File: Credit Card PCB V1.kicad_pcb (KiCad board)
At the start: 2 copper layers, 85.5 x 54 mm, 53 parts, among them J1 USB_C_Receptacle_USB2.0, SW0 SW_Push, SW1 RotaryEncoder, U1 USBLC6-2SC6, U2 ATmega32U2-A, Y1 16MHz

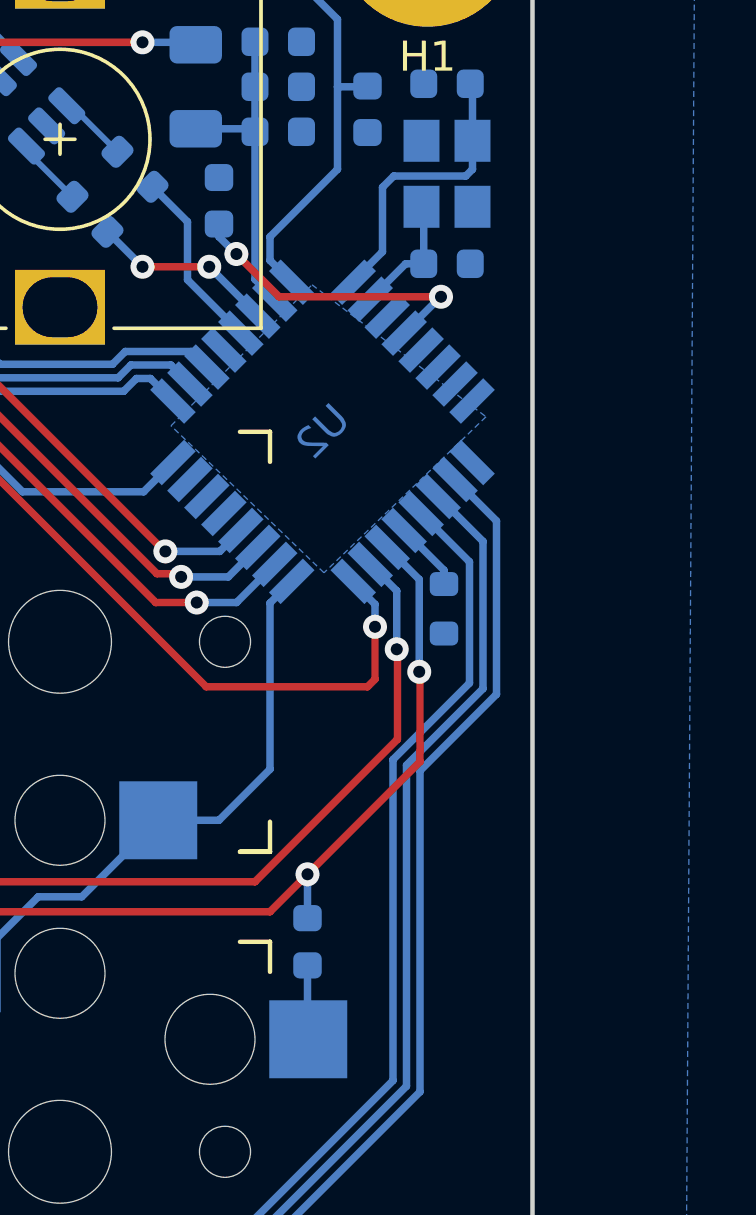
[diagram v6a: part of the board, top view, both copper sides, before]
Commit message: Adding slikscreen logo
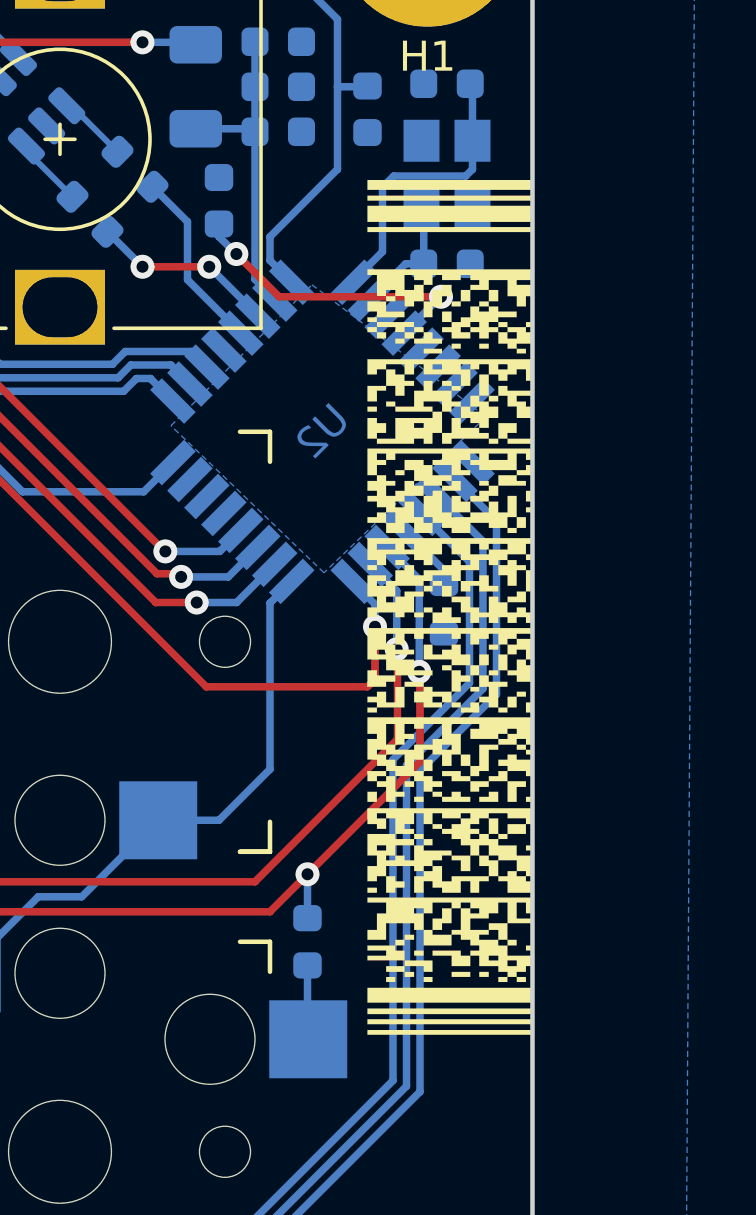
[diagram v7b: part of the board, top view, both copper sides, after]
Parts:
- added G***: LOGO, Passport V1.0, F.Cu at (167.0, 91.5)
